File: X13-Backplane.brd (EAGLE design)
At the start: 86.4 x 139.3 mm, 36 parts, among them J1 PXC-PTSM-04-RA-1778641, J2 PXC-PTSM-04-RA-1778641, J3 PXC-8-RA-1778683, J4 PXC-PTSM-04-RA-1778641, J5 PXC-PTSM-04-RA-1778641, J6 284512-4, J8 PXC-8-RA-1778683

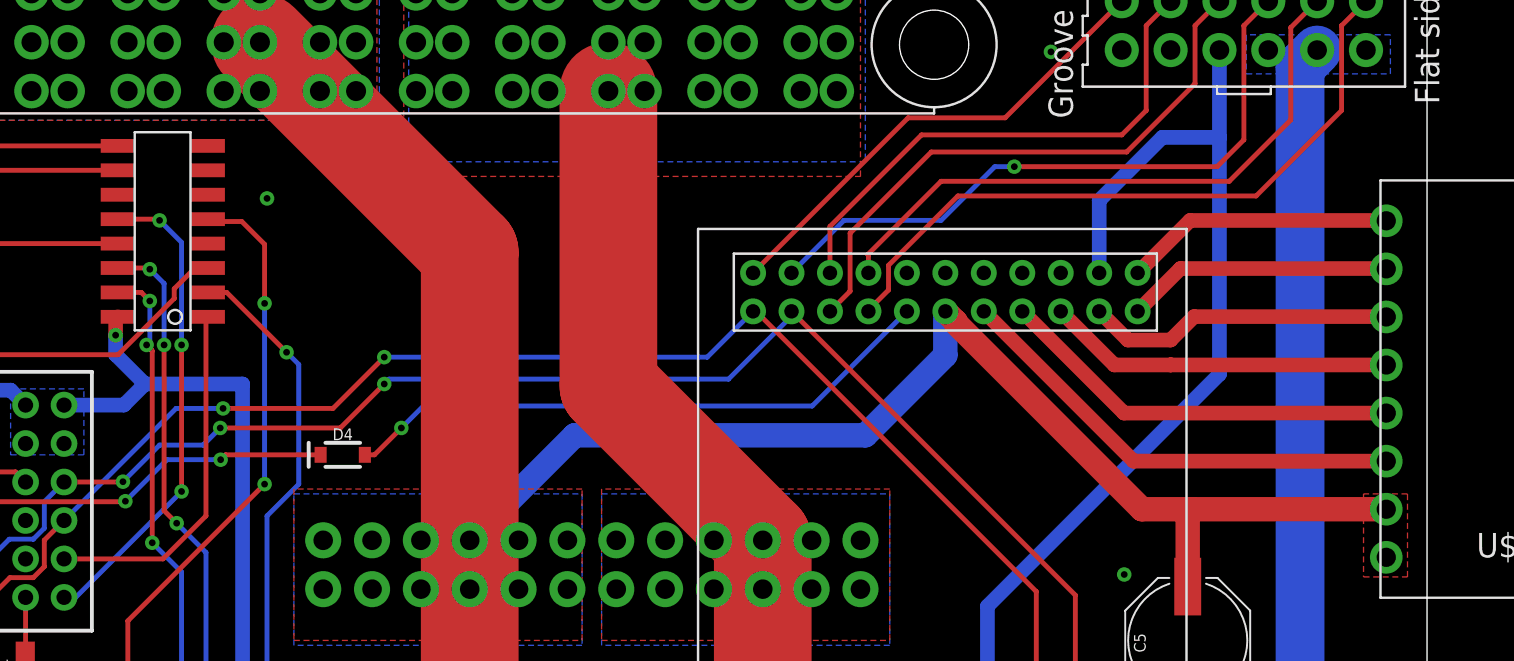
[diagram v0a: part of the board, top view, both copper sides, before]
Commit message: added swclk/swdio signals to solenoid board
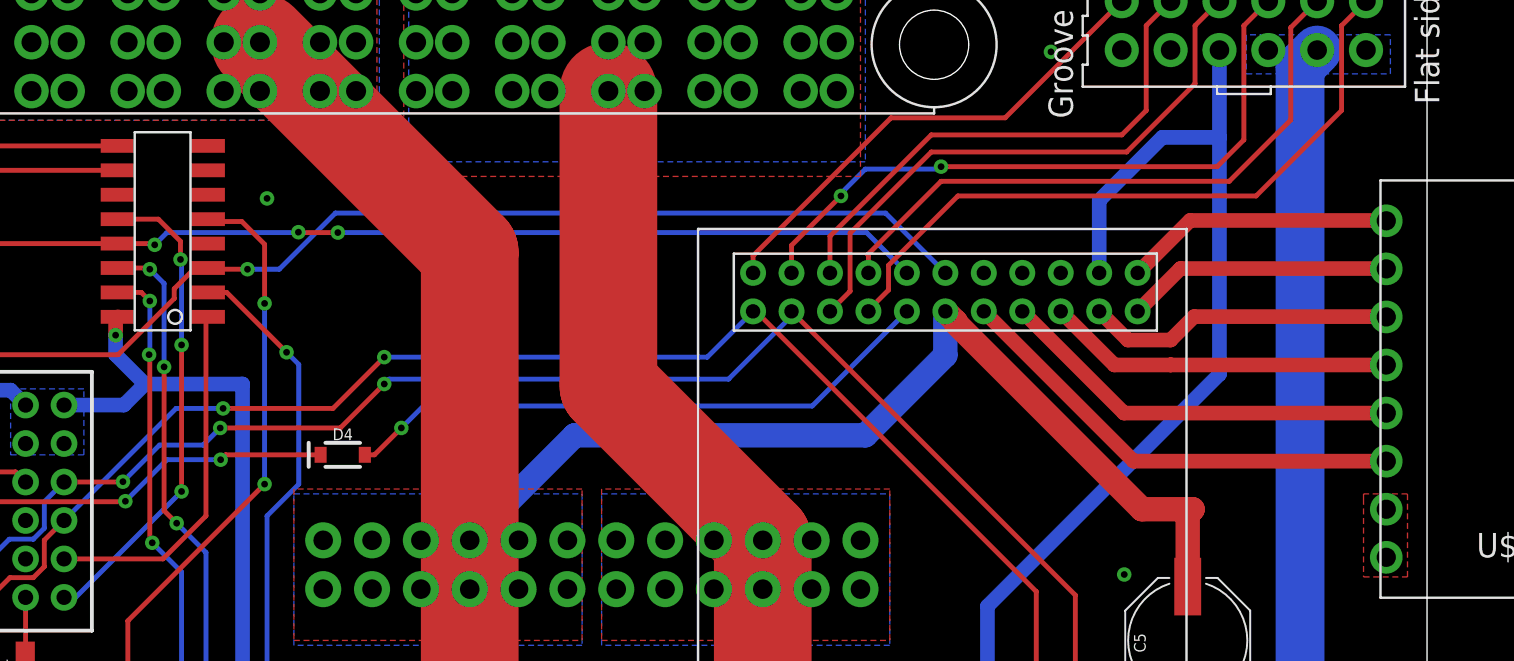
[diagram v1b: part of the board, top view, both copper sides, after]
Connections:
- net GND: no longer U$4.12
- net SWCLK_IN: now also U$4.14
- net SWDIO_IN: now also U$4.12
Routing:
- net SWCLK_IN: track 22.8 -> 65.0 mm, vias 0 -> 3
- net SWDIO_IN: track 29.0 -> 70.3 mm, vias 0 -> 1
- net 12V: track 179.4 -> 169.3 mm
- net CLK: track 34.1 -> 35.0 mm, vias 1 -> 2
- net DATA: track 25.0 -> 25.5 mm

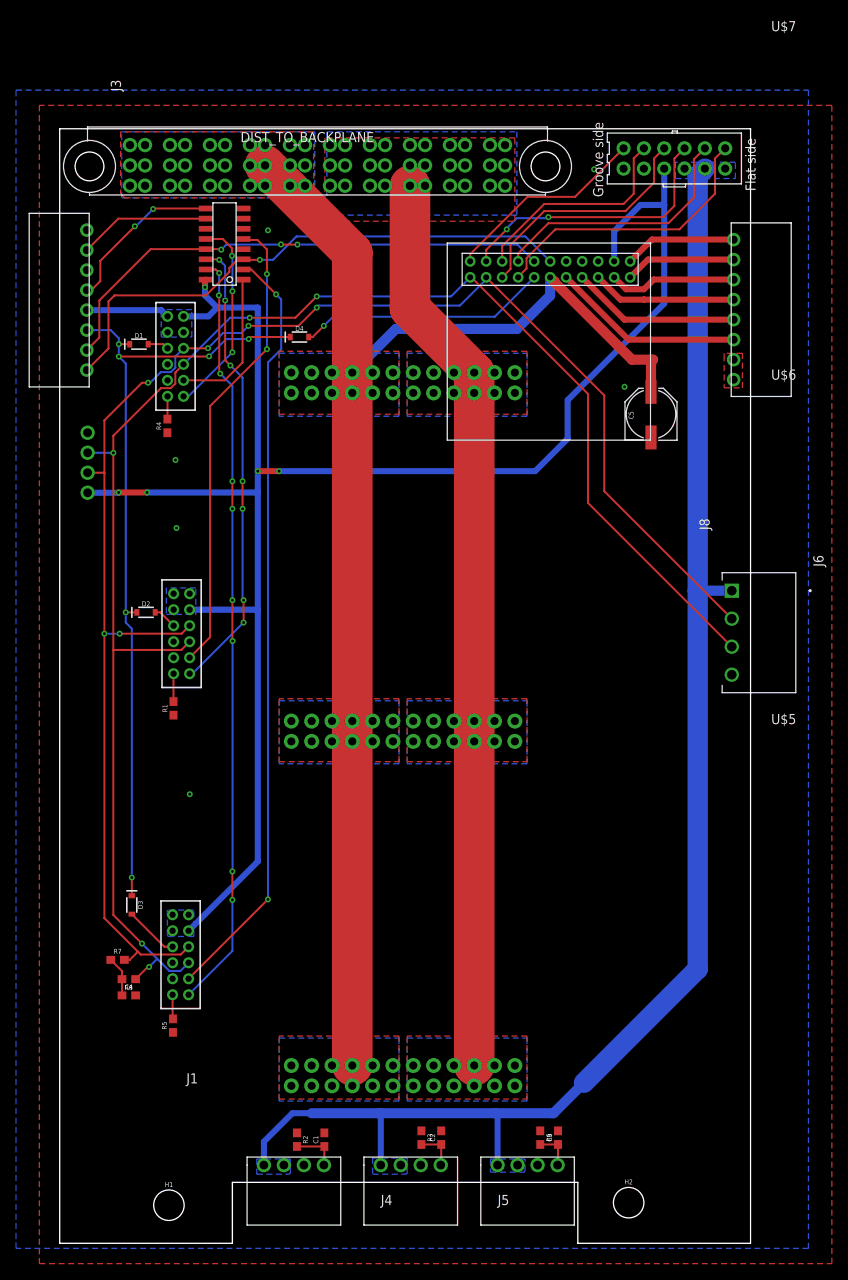
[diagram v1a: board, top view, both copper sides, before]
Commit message: added cutouts, adjusted gnd
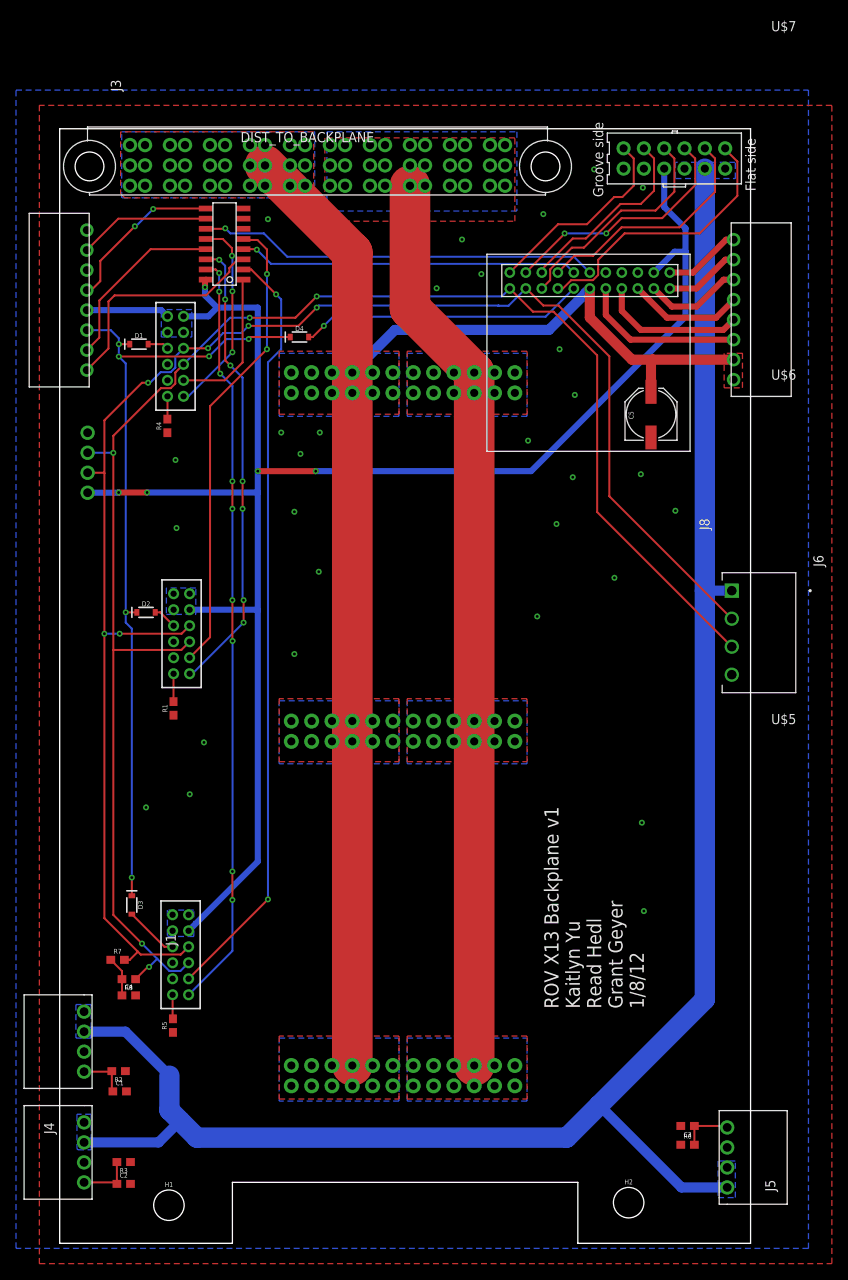
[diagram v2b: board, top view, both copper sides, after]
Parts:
- moved C2 40.1 mm to (15.6, 7.43), turned to 0 degrees
- moved J4 37.5 mm to (10.7, 15.1), turned to 270 degrees
- moved R3 37.3 mm to (15.6, 10.2), turned to 180 degrees
- moved J1 29.5 mm to (10.7, 29.0), turned to 270 degrees
- moved J5 28.8 mm to (91.1, 6.99), turned to 90 degrees
- moved C1 26.3 mm to (15.1, 19.0), turned to 0 degrees
- moved R2 23.9 mm to (15.0, 21.5), turned to 180 degrees
- moved R6 18.4 mm to (86.1, 12.3), turned to 0 degrees
- moved C3 16.3 mm to (86.1, 14.7), turned to 180 degrees
- moved U$4 5.15 mm to (83.9, 121.3)
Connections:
- new net SWCLK_4: MUX.11, U$4.12
- new net SWDIO_4: MUX.4, U$4.14
- net SWCLK_IN: no longer U$4.14
- net SWDIO_IN: no longer U$4.12
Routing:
- net SWCLK_4: track 0.00 -> 50.3 mm, vias 0 -> 1
- net 5V: track 183.8 -> 233.4 mm
- net SWDIO_4: track 0.00 -> 42.5 mm, vias 0 -> 1
- net SWCLK_IN: track 65.0 -> 22.8 mm, vias 3 -> 0
- net SWDIO_IN: track 70.3 -> 29.0 mm, vias 1 -> 0
- net 12V: track 169.3 -> 179.0 mm
- net 3.3V: track 226.2 -> 221.8 mm
- net SOL2_1: track 13.9 -> 9.47 mm
- net SOL1_1: track 14.1 -> 9.68 mm
- net NRST_4: track 31.3 -> 35.7 mm
- net CLK: track 35.0 -> 30.9 mm
- net SOL3_1: track 16.1 -> 12.3 mm
- net SOL4_1: track 18.1 -> 14.5 mm
- net SOL6_1: track 24.2 -> 20.6 mm
- net ALERT_1: track 27.3 -> 24.3 mm
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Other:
- board text added: "ROV X13 Backplane v1 Kaitlyn Yu Read Hedl Grant Geyer 1/8/12"

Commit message: updated board
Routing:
- net 3.3V: track 221.8 -> 225.7 mm
- net 12VGND: track 113.3 -> 116.4 mm
- net 12V: track 179.0 -> 181.8 mm
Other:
- outline, holes or cut-outs redrawn
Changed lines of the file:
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@@
 Grant Geyer
 1/8/12</text>
+<wire x1="49.784" y1="88.773" x2="49.784" y2="101.473" width="0" layer="20"/>
+<wire x1="49.784" y1="101.473" x2="54.102" y2="101.473" width="0" layer="20"/>
+<wire x1="54.102" y1="101.473" x2="54.102" y2="88.773" width="0" layer="20"/>
+<wire x1="54.102" y1="88.773" x2="49.784" y2="88.773" width="0" layer="20"/>
+<wire x1="49.403" y1="42.545" x2="49.403" y2="55.245" width="0" layer="20"/>
+<wire x1="49.403" y1="55.245" x2="53.721" y2="55.245" width="0" layer="20"/>
+<wire x1="53.721" y1="55.245" x2="53.721" y2="42.545" width="0" layer="20"/>
+<wire x1="53.721" y1="42.545" x2="49.403" y2="42.545" width="0" layer="20"/>
 </plain>
 <attributes>
@@
 <via x="27.559" y="122.936" extent="1-16" drill="0.35"/>
 <wire x1="27.559" y1="122.936" x2="28.3012" y2="122.1938" width="0.254" layer="16"/>
-<wire x1="28.3012" y1="122.1938" x2="28.3012" y2="117.983" width="0.254" layer="16"/>
-<via x="28.3012" y="117.983" extent="1-16" drill="0.35"/>
-<wire x1="28.3012" y1="117.983" x2="28.3012" y2="110.3828" width="0.254" layer="1"/>
+<wire x1="28.3012" y1="122.1938" x2="28.3012" y2="118.364" width="0.254" layer="16"/>
+<via x="28.3012" y="118.364" extent="1-16" drill="0.35"/>
+<wire x1="28.3012" y1="118.364" x2="28.3012" y2="110.3828" width="0.254" layer="1"/>
 <wire x1="28.3012" y1="110.3828" x2="28.956" y2="109.728" width="0.254" layer="1"/>
 <via x="28.956" y="109.728" extent="1-16" drill="0.35"/>
@@
 <contactref element="U$3" pad="4"/>
 <wire x1="32.385" y1="47.72" x2="23.733" y2="39.068" width="0.762" layer="16"/>
-<wire x1="32.385" y1="116.967" x2="32.385" y2="96.52" width="0.762" layer="16"/>
-<wire x1="32.385" y1="96.52" x2="32.385" y2="93.853" width="0.762" layer="16"/>
-<wire x1="32.385" y1="93.853" x2="32.385" y2="79.121" width="0.762" layer="16"/>
+<wire x1="32.385" y1="93.853" x2="32.385" y2="87.122" width="0.762" layer="16"/>
+<wire x1="32.385" y1="87.122" x2="32.385" y2="79.121" width="0.762" layer="16"/>
 <wire x1="32.385" y1="79.121" x2="32.385" y2="47.72" width="0.762" layer="16"/>
 <wire x1="23.86" y1="79.2" x2="32.306" y2="79.2" width="0.762" layer="16"/>
@@
 <wire x1="11.01" y1="116.64625" x2="20.32275" y2="116.64625" width="0.762" layer="16"/>
 <wire x1="20.32275" y1="116.64625" x2="21.098" y2="115.871" width="0.762" layer="16"/>
-<wire x1="32.385" y1="116.967" x2="27.305" y2="116.967" width="0.762" layer="16"/>
-<wire x1="27.305" y1="116.967" x2="25.781" y2="118.491" width="0.762" layer="16"/>
+<wire x1="32.385" y1="117.348" x2="26.924" y2="117.348" width="0.762" layer="16"/>
+<wire x1="26.924" y1="117.348" x2="25.781" y2="118.491" width="0.762" layer="16"/>
 <wire x1="25.781" y1="118.491" x2="25.781" y2="119.507" width="0.762" layer="16"/>
 <via x="25.781" y="119.507" extent="1-16" drill="0.35"/>
@@
 <via x="18.542" y="93.853" extent="1-16" drill="0.35"/>
 <wire x1="18.542" y1="93.853" x2="32.385" y2="93.853" width="0.762" layer="16"/>
-<wire x1="23.098" y1="115.871" x2="26.209" y2="115.871" width="0.762" layer="16"/>
-<wire x1="26.209" y1="115.871" x2="27.305" y2="116.967" width="0.762" layer="16"/>
-<wire x1="39.624" y1="96.52" x2="66.548" y2="96.52" width="0.762" layer="16"/>
-<via x="39.624" y="96.52" extent="1-16" drill="0.35"/>
-<wire x1="39.624" y1="96.52" x2="32.385" y2="96.52" width="0.762" layer="1"/>
-<via x="32.385" y="96.52" extent="1-16" drill="0.35"/>
+<wire x1="23.098" y1="115.871" x2="25.447" y2="115.871" width="0.762" layer="16"/>
+<wire x1="25.447" y1="115.871" x2="26.924" y2="117.348" width="0.762" layer="16"/>
+<via x="39.878" y="87.122" extent="1-16" drill="0.35"/>
 <wire x1="85.852" y1="115.824" x2="85.852" y2="123.952" width="0.762" layer="16"/>
-<wire x1="66.548" y1="96.52" x2="85.852" y2="115.824" width="0.762" layer="16"/>
+<wire x1="57.15" y1="87.122" x2="85.852" y2="115.824" width="0.762" layer="16"/>
 <wire x1="83.185" y1="134.33425" x2="83.185" y2="129.54" width="0.762" layer="16"/>
 <wire x1="83.185" y1="129.54" x2="85.852" y2="126.873" width="0.762" layer="16"/>
@@
 <wire x1="84.487" y1="123.952" x2="85.852" y2="123.952" width="0.762" layer="16"/>
 <wire x1="81.8835" y1="121.3485" x2="84.487" y2="123.952" width="0.762" layer="16"/>
+<wire x1="39.878" y1="87.122" x2="32.385" y2="87.122" width="0.762" layer="1"/>
+<via x="32.385" y="87.122" extent="1-16" drill="0.35"/>
+<wire x1="39.878" y1="87.122" x2="57.15" y2="87.122" width="0.762" layer="16"/>
+<wire x1="32.385" y1="93.853" x2="32.385" y2="117.348" width="0.762" layer="16"/>
+<wire x1="21.098" y1="113.871" x2="23.098" y2="113.871" width="0" layer="19" extent="1-1"/>
+<wire x1="21.098" y1="115.871" x2="21.098" y2="113.871" width="0" layer="19" extent="1-1"/>
+<wire x1="23.098" y1="115.871" x2="23.098" y2="113.871" width="0" layer="19" extent="1-1"/>
+<wire x1="23.86" y1="81.2" x2="23.86" y2="79.2" width="0" layer="19" extent="1-1"/>
+<wire x1="21.86" y1="81.2" x2="23.86" y2="81.2" width="0" layer="19" extent="1-1"/>
+<wire x1="21.86" y1="79.2" x2="23.86" y2="79.2" width="0" layer="19" extent="1-1"/>
+<wire x1="23.733" y1="41.068" x2="23.733" y2="39.068" width="0" layer="19" extent="1-1"/>
+<wire x1="21.733" y1="41.068" x2="23.733" y2="41.068" width="0" layer="19" extent="1-1"/>
+<wire x1="21.733" y1="39.068" x2="23.733" y2="39.068" width="0" layer="19" extent="1-1"/>
 </signal>
 <signal name="CAN_H">
@@
 <vertex x="35.052" y="25.654"/>
 </polygon>
-<wire x1="44.196" y1="108.839" x2="49.53" y2="114.173" width="1.27" layer="16"/>
+<wire x1="44.196" y1="108.839" x2="44.196" y2="113.538" width="1.27" layer="16"/>
+<wire x1="45.212" y1="114.554" x2="44.196" y2="113.538" width="1.27" layer="16"/>
 <wire x1="79.15335" y1="110.4545" x2="81.788" y2="110.4545" width="1.27" layer="1"/>
 <polygon width="0.762" layer="1">
@@
 <wire x1="73.3459" y1="118.74275" x2="73.3459" y2="118.8109" width="1.27" layer="16"/>
 <wire x1="73.3459" y1="118.8109" x2="73.8835" y2="119.3485" width="1.27" layer="16"/>
-<wire x1="68.77615" y1="114.173" x2="73.3459" y2="118.74275" width="1.27" layer="16"/>
-<wire x1="49.53" y1="114.173" x2="68.77615" y2="114.173" width="1.27" layer="16"/>
+<wire x1="69.15715" y1="114.554" x2="73.3459" y2="118.74275" width="1.27" layer="16"/>
+<wire x1="45.212" y1="114.554" x2="69.15715" y2="114.554" width="1.27" layer="16"/>
 <wire x1="73.8835" y1="115.72435" x2="73.8835" y2="119.3485" width="1.27" layer="1"/>
 </signal>
@@
 <wire x1="51.40625" y1="132.20125" x2="51.40625" y2="116.86875" width="5.08" layer="1"/>
 <wire x1="51.40625" y1="116.86875" x2="59.436" y2="108.839" width="5.08" layer="1"/>
-<wire x1="59.436" y1="108.839" x2="59.436" y2="65.278" width="5.08" layer="1"/>
+<wire x1="59.436" y1="108.839" x2="63.119" y2="105.156" width="5.08" layer="1"/>
+<wire x1="63.119" y1="105.156" x2="63.119" y2="68.961" width="5.08" layer="1"/>
+<wire x1="63.119" y1="68.961" x2="59.436" y2="65.278" width="5.08" layer="1"/>
 <wire x1="59.436" y1="65.278" x2="59.436" y2="22.225" width="5.08" layer="1"/>
 <polygon width="0.762" layer="1">
